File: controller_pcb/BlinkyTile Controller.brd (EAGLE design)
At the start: 40 x 25 mm, 31 parts, among them CN1 Battery, CON1 USB_MICROSMT+THRUHULE, CON2 M05X2NO_SILK, CON3 LED_OUT, CON4 M01PTH, Q1 16MHz, SW1 BUTTON_1, SW2 BUTTON_2, T1 SSM3J328R,LF, U1 MK20D--VFM5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

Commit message: Controller pcb, as fixed
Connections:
- removed net SW2: U1.30
- net BUTTON2: now also U1.30
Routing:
- net BUTTON2: track 8.30 -> 14.7 mm
- net SW2: track 5.53 -> 0.00 mm
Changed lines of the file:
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@@
 <layer number="14" name="Route14" color="1" fill="6" visible="no" active="no"/>
 <layer number="15" name="Route15" color="4" fill="6" visible="no" active="no"/>
-<layer number="16" name="Bottom" color="1" fill="1" visible="no" active="yes"/>
-<layer number="17" name="Pads" color="2" fill="1" visible="no" active="yes"/>
-<layer number="18" name="Vias" color="2" fill="1" visible="no" active="yes"/>
-<layer number="19" name="Unrouted" color="6" fill="1" visible="no" active="yes"/>
+<layer number="16" name="Bottom" color="1" fill="1" visible="yes" active="yes"/>
+<layer number="17" name="Pads" color="2" fill="1" visible="yes" active="yes"/>
+<layer number="18" name="Vias" color="2" fill="1" visible="yes" active="yes"/>
+<layer number="19" name="Unrouted" color="6" fill="1" visible="yes" active="yes"/>
 <layer number="20" name="Dimension" color="15" fill="1" visible="yes" active="yes"/>
-<layer number="21" name="tPlace" color="7" fill="1" visible="no" active="yes"/>
-<layer number="22" name="bPlace" color="7" fill="1" visible="no" active="yes"/>
+<layer number="21" name="tPlace" color="7" fill="1" visible="yes" active="yes"/>
+<layer number="22" name="bPlace" color="7" fill="1" visible="yes" active="yes"/>
 <layer number="23" name="tOrigins" color="15" fill="1" visible="yes" active="yes"/>
-<layer number="24" name="bOrigins" color="15" fill="1" visible="no" active="yes"/>
+<layer number="24" name="bOrigins" color="15" fill="1" visible="yes" active="yes"/>
 <layer number="25" name="tNames" color="7" fill="1" visible="yes" active="yes"/>
-<layer number="26" name="bNames" color="7" fill="1" visible="no" active="yes"/>
+<layer number="26" name="bNames" color="7" fill="1" visible="yes" active="yes"/>
 <layer number="27" name="tValues" color="7" fill="1" visible="no" active="yes"/>
 <layer number="28" name="bValues" color="7" fill="1" visible="no" active="yes"/>
@@
 <layer number="39" name="tKeepout" color="4" fill="11" visible="no" active="yes"/>
 <layer number="40" name="bKeepout" color="1" fill="11" visible="no" active="yes"/>
-<layer number="41" name="tRestrict" color="4" fill="10" visible="no" active="yes"/>
-<layer number="42" name="bRestrict" color="1" fill="10" visible="no" active="yes"/>
+<layer number="41" name="tRestrict" color="4" fill="10" visible="yes" active="yes"/>
+<layer number="42" name="bRestrict" color="1" fill="10" visible="yes" active="yes"/>
 <layer number="43" name="vRestrict" color="2" fill="10" visible="no" active="yes"/>
 <layer number="44" name="Drills" color="7" fill="1" visible="no" active="yes"/>
 <layer number="45" name="Holes" color="7" fill="1" visible="no" active="yes"/>
 <layer number="46" name="Milling" color="3" fill="1" visible="no" active="yes"/>
-<layer number="47" name="Measures" color="7" fill="1" visible="no" active="yes"/>
-<layer number="48" name="Document" color="7" fill="1" visible="no" active="yes"/>
+<layer number="47" name="Measures" color="7" fill="1" visible="yes" active="yes"/>
+<layer number="48" name="Document" color="7" fill="1" visible="yes" active="yes"/>
 <layer number="49" name="Reference" color="7" fill="1" visible="no" active="yes"/>
 <layer number="50" name="dxf" color="7" fill="1" visible="no" active="no"/>
@@
 <layer number="199" name="Contour" color="7" fill="1" visible="no" active="yes"/>
 <layer number="200" name="b_bitmap" color="15" fill="1" visible="no" active="yes"/>
-<layer number="201" name="t_bitmap" color="15" fill="1" visible="no" active="yes"/>
+<layer number="201" name="t_bitmap" color="15" fill="1" visible="yes" active="yes"/>
 <layer number="202" name="202bmp" color="3" fill="10" visible="no" active="yes"/>
 <layer number="203" name="203bmp" color="4" fill="10" visible="no" active="yes"/>
@@
 <wire x1="12" y1="15.5" x2="12.5" y2="16" width="0.2032" layer="1"/>
 </signal>
-<signal name="SW2">
-<contactref element="U1" pad="30"/>
-<wire x1="17.5" y1="15.275" x2="17.5" y2="16.496" width="0.2032" layer="1"/>
-<wire x1="17.5" y1="16.496" x2="16.996" y2="17" width="0.2032" layer="1"/>
-<wire x1="16.996" y1="17" x2="14.25" y2="17" width="0.2032" layer="1"/>
-<wire x1="14.25" y1="17" x2="13.65" y2="17.6" width="0.2032" layer="1"/>
-</signal>
 <signal name="DATA_OUT">
 <contactref element="U4" pad="2"/>
@@
 <wire x1="6.5" y1="18.75" x2="6.5" y2="18.5" width="0.2032" layer="1"/>
 <wire x1="6.5" y1="18.5" x2="5.85" y2="18.5" width="0.2032" layer="1"/>
+<contactref element="U1" pad="30"/>
+<wire x1="17.5" y1="15.275" x2="17.5" y2="16.496" width="0.2032" layer="1"/>
+<wire x1="17.5" y1="16.496" x2="16.996" y2="17" width="0.2032" layer="1"/>
+<wire x1="16.996" y1="17" x2="14.25" y2="17" width="0.2032" layer="1"/>
+<wire x1="14.25" y1="17" x2="13.65" y2="17.6" width="0.2032" layer="1"/>
+<wire x1="13.65" y1="17.6" x2="13.65" y2="18.5" width="0.2032" layer="1"/>
 </signal>
 </signals>

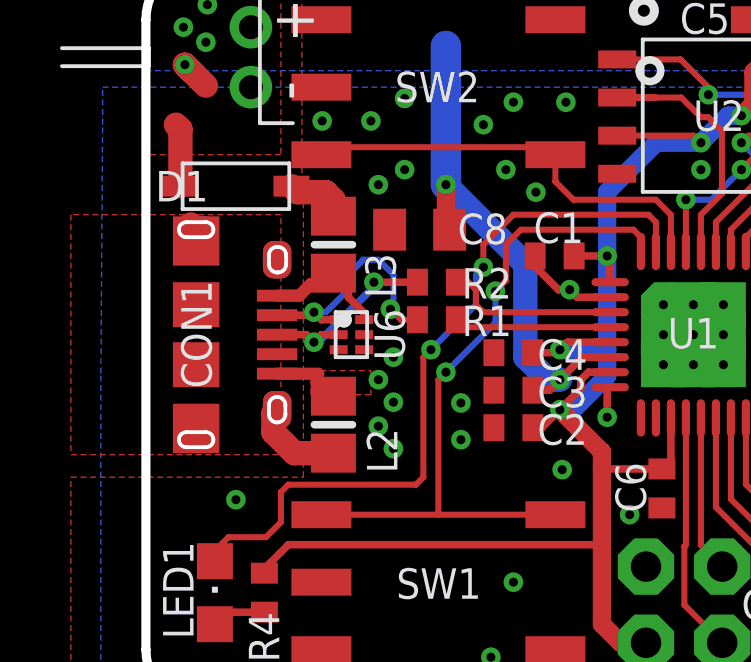
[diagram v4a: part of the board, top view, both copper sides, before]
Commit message: Control Board: make USB pads longer, update silkscreen (RevE)
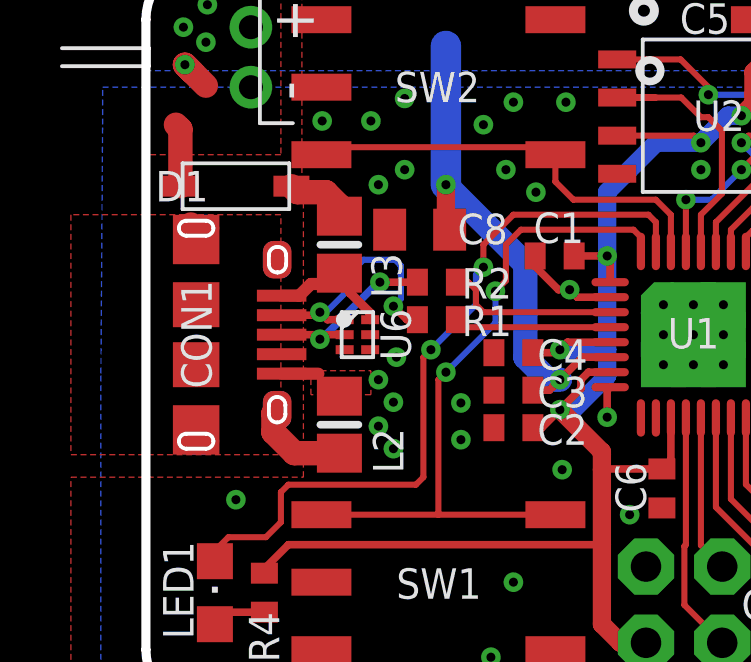
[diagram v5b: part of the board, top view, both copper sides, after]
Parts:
- moved L2 0.20 mm to (6.45, 9.50)
- moved L3 0.20 mm to (6.45, 15.5)
- moved U6 0.20 mm to (7.05, 12.5)
